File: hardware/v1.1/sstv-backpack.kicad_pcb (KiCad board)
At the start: 2 copper layers, 38.1 x 63.5 mm, 25 parts, among them J1 Conn_01x03_Pin, J2 Conn_01x02_Pin, J3 2172034-1, SW1 SW_Push, SW2 SLW-1276864-4A-D, U1 ESP32-CAM, U2 FT231XS

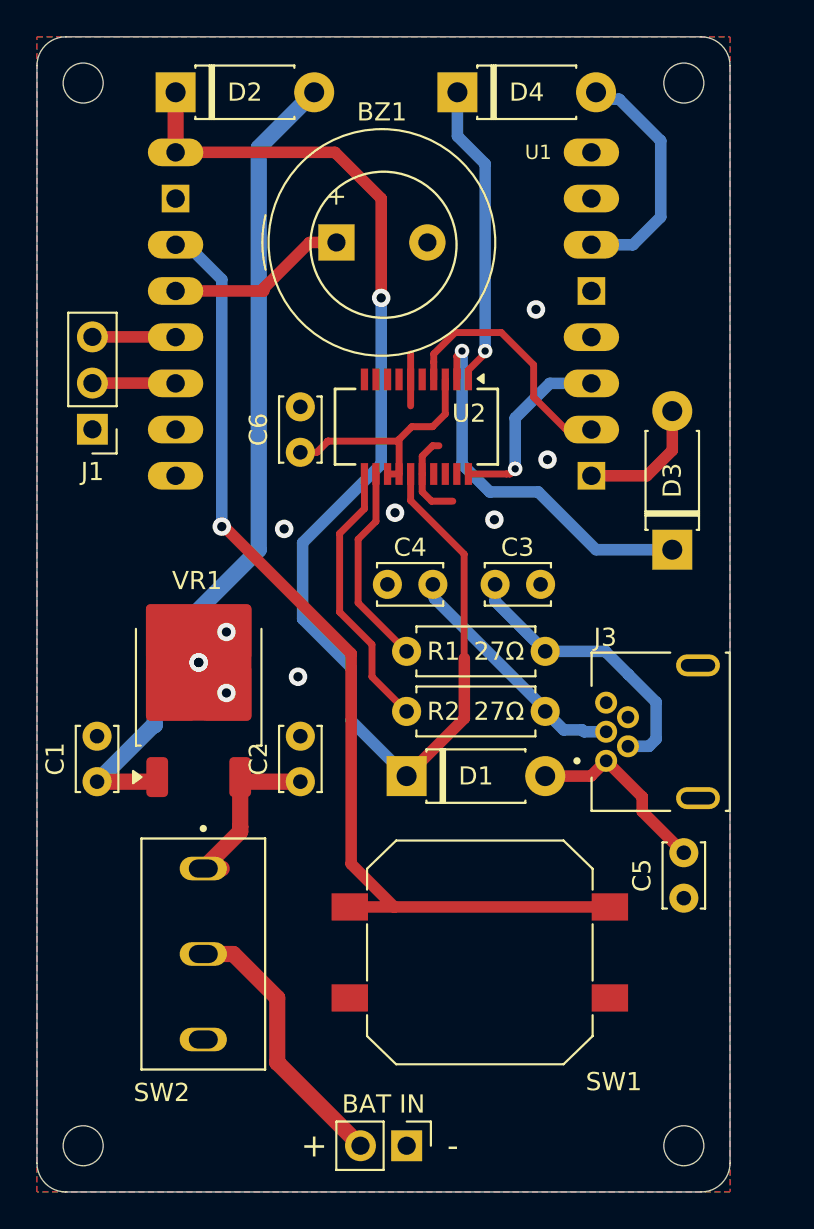
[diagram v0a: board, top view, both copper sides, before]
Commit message: Swap v1.1 to USB-C and add v1.2
Swapped v1.1 to USB-C from USB Mini B, added the TX transmit transistor to hopefully fix the TX hang, and added the WIP files for v1.2
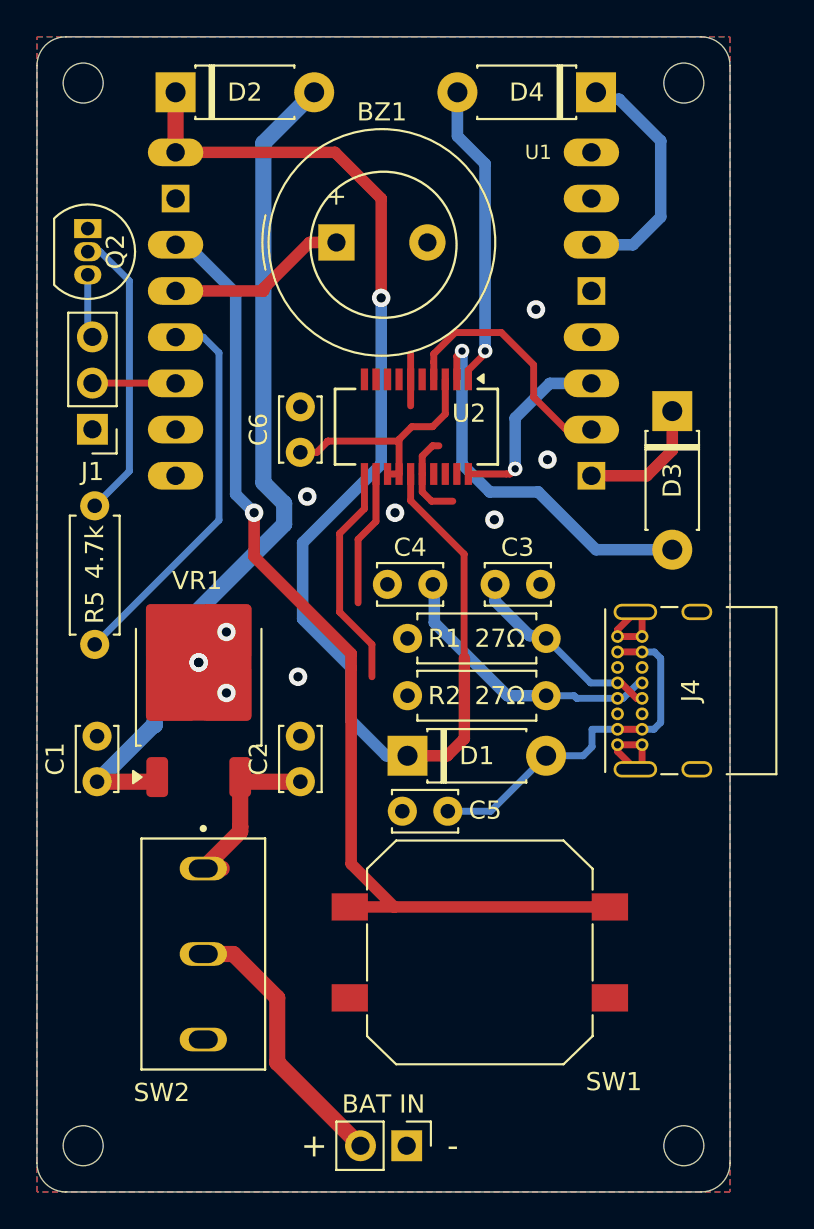
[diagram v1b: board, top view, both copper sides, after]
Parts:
- removed J3: 2172034-1, 2172034-1:TE_2172034-1
- added J4: USB_C_Receptacle_USB2.0_14P, Connector_USB:USB_C_Receptacle_GCT_USB4085, F.Cu at (171.6, 102.4)
- added Q2: 2N3904, Package_TO_SOT_THT:TO-92_Inline, F.Cu at (142.5, 74.0)
- added R5: 4.7k, Resistor_THT:R_Axial_DIN0207_L6.3mm_D2.5mm_P7.62mm_Horizontal, F.Cu at (142.9, 96.9)
- moved C5 16.2 mm to (159.8, 106.1), turned to 0 degrees
- moved D3 7.62 mm to (174.6, 84.1), turned to -90 degrees
- moved D4 7.62 mm to (170.4, 66.5), turned to 180 degrees
- moved D1 1.12 mm to (160.1, 103.0)
- moved R2 0.87 mm to (167.7, 99.7)
- moved R1 0.71 mm to (167.7, 96.6)
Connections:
- net Net-(D2-A) renamed /5VO
- net Net-(J3-D+) renamed /D+
- net Net-(J3-D-) renamed /D-
- D3 pad 1: RTS -> Net-(D3-K)
- D3 pad 2: Net-(D3-A) -> RTS
- D4 pad 1: DTR -> Net-(D4-K)
- D4 pad 2: Net-(D4-A) -> DTR
- J1 pad 3: /PTT -> PTT
- U1 pad P$1: Net-(D3-A) -> Net-(D3-K)
- U1 pad P$13: /PTT -> PTT_TRIG
- U1 pad P$6: Net-(D4-A) -> Net-(D4-K)
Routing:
- net PTT_TRIG: track 0.00 -> 21.6 mm
- net Net-(Q2-B): track 0.00 -> 16.1 mm
- net Net-(D4-K): track 0.00 -> 13.3 mm
- net Net-(D4-A): track 13.3 -> 0.00 mm
- net /5VUSB: track 10.5 -> 20.3 mm
- net GND: track 7.87 -> 17.1 mm
- net Net-(D3-K): track 0.00 -> 7.18 mm
- net Net-(D3-A): track 7.18 -> 0.00 mm
- net /D-: track 15.8 -> 11.2 mm
- net /PTT: track 4.58 -> 0.00 mm
- net Net-(U2-USBDM): track 11.3 -> 7.49 mm
- net PTT: track 0.00 -> 3.52 mm
- net Net-(U2-USBDP): track 15.1 -> 12.4 mm
- net /D+: track 13.3 -> 15.6 mm
- net /5VO: track 46.3 -> 47.2 mm

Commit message: Update v1.1 gerber and BOM
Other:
- board text added: "v1.1"
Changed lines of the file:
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@@
 			(drillshape 0)
 			(scaleselection 1)
-			(outputdirectory "gerber/")
+			(outputdirectory "gerbers/")
 		)
 	)
@@
 	)
 	(gr_text "By Preston - W7PBC"
-		(at 173.8376 114.8588 0)
+		(at 176.7332 112.6744 0)
 		(layer "B.SilkS")
 		(effects
@@
 	)
 	(gr_text "github.com/vaugerbird/\nsstv-backpack"
-		(at 164.211 119.761 0)
+		(at 159.3596 118.9736 0)
 		(layer "B.SilkS")
 		(effects
@@
 	)
 	(gr_text "SSTV Backpack"
-		(at 174.4472 112.6744 0)
+		(at 176.8348 109.982 0)
 		(layer "B.SilkS")
 		(effects
@@
 		)
 	)
+	(gr_text "v1.1"
+		(at 176.7332 115.316 0)
+		(layer "B.SilkS")
+		(effects
+			(font
+				(size 1.27 1.27)
+				(thickness 0.254)
+				(bold yes)
+			)
+			(justify left bottom mirror)
+		)
+	)

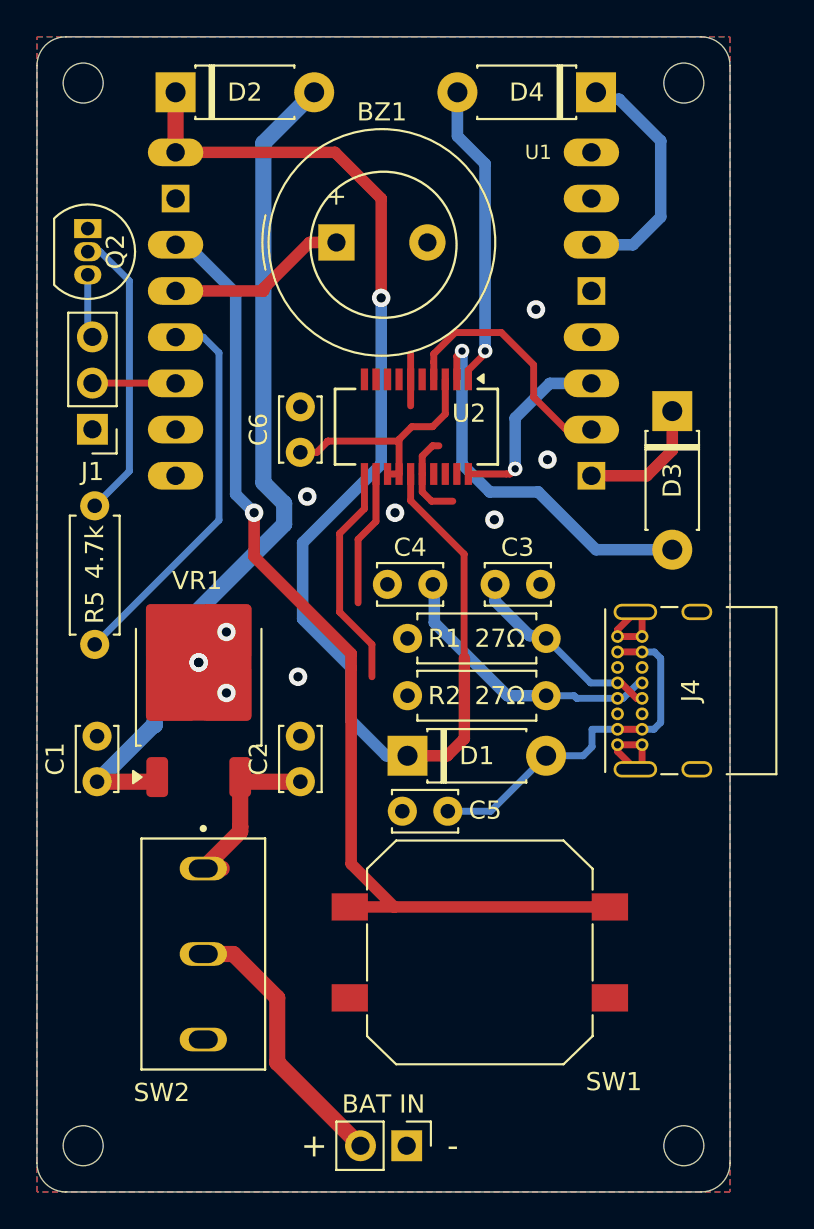
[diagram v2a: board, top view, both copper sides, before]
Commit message: Fix PCB and add USB-C to case
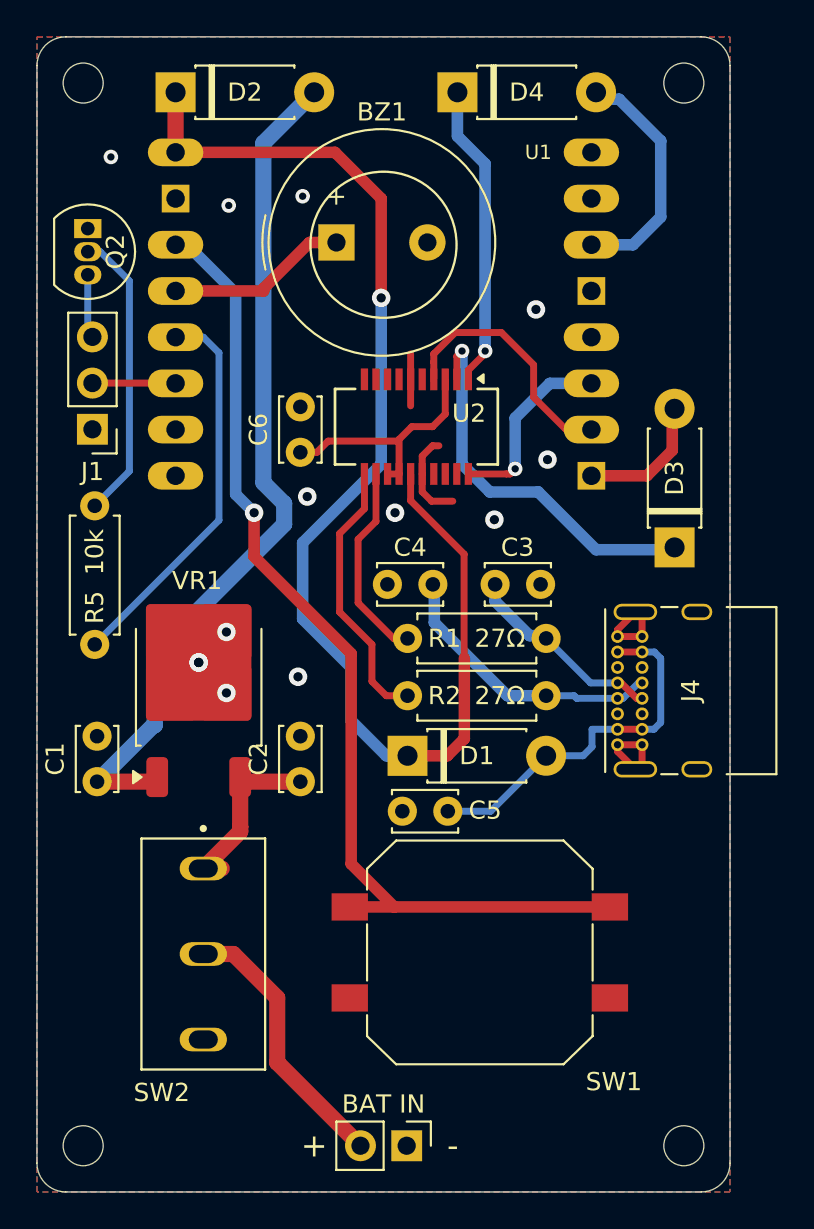
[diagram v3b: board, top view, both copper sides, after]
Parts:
- R5: value 4.7k -> 10k
- moved D4 7.62 mm to (162.8, 66.5), turned to 0 degrees
- moved D3 7.49 mm to (174.8, 91.6), turned to 90 degrees
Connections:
- D3 pad 1: Net-(D3-K) -> RTS
- D3 pad 2: RTS -> Net-(D3-A)
- D4 pad 1: Net-(D4-K) -> DTR
- D4 pad 2: DTR -> Net-(D4-A)
- U1 pad P$1: Net-(D3-K) -> Net-(D3-A)
- U1 pad P$6: Net-(D4-K) -> Net-(D4-A)
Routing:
- net Net-(D4-K): track 13.3 -> 0.00 mm
- net Net-(D4-A): track 0.00 -> 13.3 mm
- net Net-(D3-K): track 7.18 -> 0.00 mm
- net Net-(D3-A): track 0.00 -> 7.18 mm
- net Net-(U2-USBDM): track 7.49 -> 11.0 mm
- net Net-(U2-USBDP): track 12.4 -> 15.0 mm
- net GND: vias 10 -> 13
